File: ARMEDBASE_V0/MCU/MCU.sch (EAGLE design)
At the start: 23 parts, among them IC1 REG1117, K1 CQ1-12V, Q2 2N3904

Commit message: mcu
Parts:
- added C3, C4: 22pF, SparkFun-Capacitors:CAP0805
- added C5: 10nF, SparkFun-Capacitors:CAP0805
- added D2: (no value), SparkFun-DiscreteSemi:DIODESMA
- added IC2: MEGA8-P, atmel:MEGA8-P
- added LOGO1: OSHW-LOGOL, SparkFun-Aesthetics:OSHW-LOGOL
- added Q1: 20Mhz, crystal:CRYSTALSM49
- added Q3: 2N3904, semicon-smd-ipc:NPN-TRANSISTOR_SOT23
- added R11, R9: 1K, SparkFun-Passives:RESISTOR0805-RES
- added S2: SWITCH-MOMENTARY-2PTH, SparkFun-Electromechanical:SWITCH-MOMENTARY-2PTH
- added SV1: 5v, con-lstb:MA04-1
- S1: device SparkFun-Electromechanical:SWITCH-SPDTSMD2 -> switch:255SB
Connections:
- new net N$1: J2.2, K12.S
- new net N$21: C3.2, IC2.PB6(XTAL1/TOSC1), Q1.2
- new net N$23: C4.2, IC2.PB7(XTAL2/TOSC2), Q1.1
- new net N$24: C5.2, IC2.PC6(/RESET), R9.2, S2.1
- new net N$5: D2.A, K11.1, Q3.C
- new net N$6: Q3.B, R11.1
- new net N$9: IC2.PD7(AIN1), R11.2
- net GND: now also C3.1, C4.1, C5.1, IC2.GND, IC2.GND@1, K12.P, Q3.E, S2.2
- net RX: now also IC2.PD0(RXD)
- net TX: now also IC2.PD1(TXD)
- net VCC12V: now also D2.C, J2.1, K11.2
- net VCC5V: now also IC2.AVCC, IC2.VCC@1, R9.1
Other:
- moved on the sheet: C1, C2, D1, IC1, J1, J2, K1, LED1, R1, R2, R3, R8

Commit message: 7805
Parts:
- removed IC1: REG1117, burr-brown:REG1117
- added IC3: (no value), SparkFun-PowerIC:V_REG_78XX-TO-220
- added X1: (no value), con-berg:PN87520
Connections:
- removed net N$1: J2.2, K12.S
- net GND: now also IC3.GND; no longer IC1.GND, K12.P
- net N$5: now also J2.1; no longer K11.1
- net VCC12V: now also IC3.IN, J2.2; no longer IC1.VIN, J2.1, K11.2
- net VCC5V: now also IC3.OUT; no longer IC1.VOUT
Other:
- moved on the sheet: C3, C4, C5, D2, IC2, J2, K1, Q1, Q3, R11, R9, S2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

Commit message: usb
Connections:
- net GND: now also X1.4
- net VCC5V: now also X1.1
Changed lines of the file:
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@@
 <part name="X1" library="con-berg" deviceset="PN87520" device=""/>
 <part name="IC3" library="SparkFun-PowerIC" deviceset="V_REG_78XX" device="-TO-220"/>
+<part name="GND4" library="SparkFun-Aesthetics" deviceset="GND" device=""/>
 </parts>
 <sheets>
@@
 <instance part="X1" gate="G$1" x="144.78" y="134.62"/>
 <instance part="IC3" gate="G$1" x="66.04" y="86.36"/>
+<instance part="GND4" gate="1" x="129.54" y="132.08" rot="R270"/>
 </instances>
 <busses>
@@
 <junction x="127" y="38.1"/>
 <junction x="157.48" y="38.1"/>
+</segment>
+<segment>
+<pinref part="X1" gate="G$1" pin="1"/>
+<wire x1="142.24" y1="139.7" x2="132.08" y2="139.7" width="0.1524" layer="91"/>
+<label x="132.08" y="139.7" size="1.778" layer="95" rot="R180" xref="yes"/>
 </segment>
 </net>
@@
 <pinref part="GND5" gate="1" pin="GND"/>
 </segment>
+<segment>
+<pinref part="GND4" gate="1" pin="GND"/>
+<pinref part="X1" gate="G$1" pin="4"/>
+<wire x1="132.08" y1="132.08" x2="142.24" y2="132.08" width="0.1524" layer="91"/>
+</segment>
 </net>

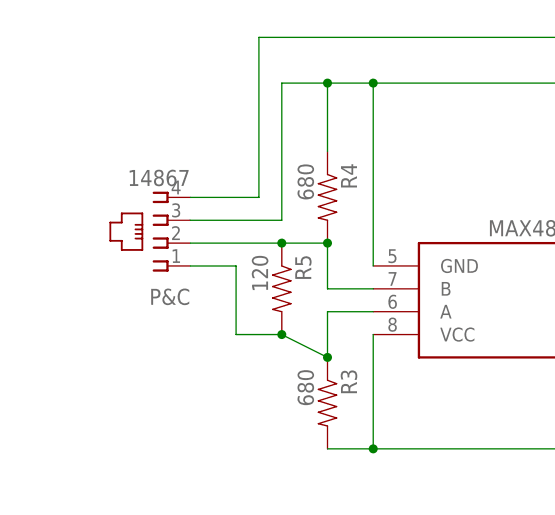
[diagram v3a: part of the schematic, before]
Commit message: modbus in-out
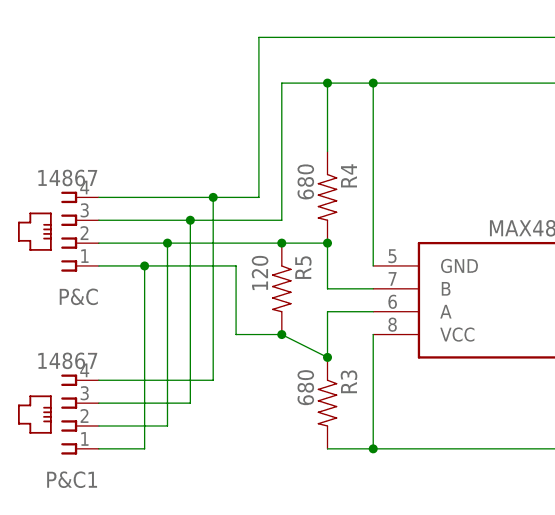
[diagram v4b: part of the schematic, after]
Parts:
- added P&C1: 14867, con-4ucon:14867
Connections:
- net GND: now also P&C1.3
- net N$7: now also P&C1.2
- net N$8: now also P&C1.1
- net VCC12V: now also P&C1.4
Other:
- moved on the sheet: P&C
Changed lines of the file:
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@@
 <part name="IC3" library="SparkFun-PowerIC" deviceset="V_REG_78XX" device="-TO-220"/>
 <part name="GND4" library="SparkFun-Aesthetics" deviceset="GND" device=""/>
+<part name="P&amp;C1" library="con-4ucon" deviceset="14867" device=""/>
 </parts>
 <sheets>
@@
 <instance part="R1" gate="G$1" x="86.36" y="15.24" rot="R270"/>
 <instance part="Q2" gate="G$1" x="78.74" y="40.64" rot="R180"/>
-<instance part="P&amp;C" gate="G$1" x="22.86" y="35.56" rot="R180"/>
+<instance part="P&amp;C" gate="G$1" x="12.7" y="35.56" rot="R180"/>
 <instance part="U$1" gate="G$1" x="60.96" y="27.94" rot="R180"/>
 <instance part="R2" gate="G$1" x="78.74" y="15.24" rot="R270"/>
@@
 <instance part="IC3" gate="G$1" x="66.04" y="86.36"/>
 <instance part="GND4" gate="1" x="129.54" y="132.08" rot="R270"/>
+<instance part="P&amp;C1" gate="G$1" x="12.7" y="15.24" rot="R180"/>
 </instances>
 <busses>
@@
 <pinref part="GND2" gate="1" pin="GND"/>
 <pinref part="P&amp;C" gate="G$1" pin="3"/>
+<wire x1="15.24" y1="35.56" x2="25.4" y2="35.56" width="0.1524" layer="91"/>
 <wire x1="25.4" y1="35.56" x2="35.56" y2="35.56" width="0.1524" layer="91"/>
 <wire x1="35.56" y1="35.56" x2="35.56" y2="50.8" width="0.1524" layer="91"/>
 <wire x1="35.56" y1="50.8" x2="40.64" y2="50.8" width="0.1524" layer="91"/>
 <junction x="40.64" y="50.8"/>
+<wire x1="25.4" y1="35.56" x2="25.4" y2="15.24" width="0.1524" layer="91"/>
+<pinref part="P&amp;C1" gate="G$1" pin="3"/>
+<wire x1="25.4" y1="15.24" x2="15.24" y2="15.24" width="0.1524" layer="91"/>
+<junction x="25.4" y="35.56"/>
 </segment>
 <segment>
@@
 <segment>
 <pinref part="P&amp;C" gate="G$1" pin="4"/>
-<wire x1="25.4" y1="38.1" x2="33.02" y2="38.1" width="0.1524" layer="91"/>
+<wire x1="15.24" y1="38.1" x2="27.94" y2="38.1" width="0.1524" layer="91"/>
 <wire x1="33.02" y1="38.1" x2="33.02" y2="55.88" width="0.1524" layer="91"/>
 <wire x1="33.02" y1="55.88" x2="104.14" y2="55.88" width="0.1524" layer="91"/>
 <label x="104.14" y="55.88" size="1.778" layer="95" xref="yes"/>
+<wire x1="33.02" y1="38.1" x2="27.94" y2="38.1" width="0.1524" layer="91"/>
+<wire x1="27.94" y1="38.1" x2="27.94" y2="17.78" width="0.1524" layer="91"/>
+<pinref part="P&amp;C1" gate="G$1" pin="4"/>
+<wire x1="27.94" y1="17.78" x2="15.24" y2="17.78" width="0.1524" layer="91"/>
+<junction x="27.94" y="38.1"/>
 </segment>
 <segment>
@@
 <wire x1="45.72" y1="27.94" x2="40.64" y2="27.94" width="0.1524" layer="91"/>
 <wire x1="40.64" y1="27.94" x2="40.64" y2="33.02" width="0.1524" layer="91"/>
-<wire x1="35.56" y1="33.02" x2="25.4" y2="33.02" width="0.1524" layer="91"/>
+<wire x1="35.56" y1="33.02" x2="22.86" y2="33.02" width="0.1524" layer="91"/>
 <pinref part="P&amp;C" gate="G$1" pin="2"/>
 <junction x="35.56" y="33.02"/>
+<wire x1="22.86" y1="33.02" x2="15.24" y2="33.02" width="0.1524" layer="91"/>
+<wire x1="22.86" y1="33.02" x2="22.86" y2="12.7" width="0.1524" layer="91"/>
+<pinref part="P&amp;C1" gate="G$1" pin="2"/>
+<wire x1="22.86" y1="12.7" x2="15.24" y2="12.7" width="0.1524" layer="91"/>
+<junction x="22.86" y="33.02"/>
 </segment>
 </net>
@@
 <junction x="40.64" y="20.32"/>
 <pinref part="P&amp;C" gate="G$1" pin="1"/>
-<wire x1="25.4" y1="30.48" x2="30.48" y2="30.48" width="0.1524" layer="91"/>
+<wire x1="15.24" y1="30.48" x2="20.32" y2="30.48" width="0.1524" layer="91"/>
+<wire x1="20.32" y1="30.48" x2="30.48" y2="30.48" width="0.1524" layer="91"/>
 <wire x1="30.48" y1="30.48" x2="30.48" y2="22.86" width="0.1524" layer="91"/>
 <junction x="35.56" y="22.86"/>
-</segment>
-</net>
+<wire x1="20.32" y1="30.48" x2="20.32" y2="10.16" width="0.1524" layer="91"/>
+<pinref part="P&amp;C1" gate="G$1" pin="1"/>
+<wire x1="20.32" y1="10.16" x2="15.24" y2="10.16" width="0.1524" layer="91"/>
+<junction x="20.32" y="30.48"/>
+</segment>
+</net>

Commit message: MCU almost
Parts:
- removed J3, J4, J5: (no value), con-amp:MTA02-156
- removed K1: CQ1-12V, relay:CQ1-12V
- added F1: 1.5A, special:FUSE
- added SV2: (no value), con-lstb:MA08-1
- added SV3, SV5: 5v, con-lstb:MA04-1
- added SV4: (no value), con-lstb:MA07-1
- Q1: value 20Mhz -> 16Mhz
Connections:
- new net KP1: IC2.PC1(ADC1), SV4.1
- new net KP2: IC2.PC0(ADC0), SV4.2
- new net KP3: IC2.PB5(SCK), SV4.3
- new net KP4: IC2.PB2(SS/OC1B), SV4.4
- new net KP5: IC2.PB1(OC1A), SV4.5
- new net KP6: IC2.PB0(ICP), SV4.6
- new net KP7: IC2.PD6(AIN0), SV4.7
- new net LCDD4: IC2.PD5(T1), SV3.4
- new net LCDD5: IC2.PD4(XCK/T0), SV3.3
- new net LCDD6: IC2.PD3(INT1), SV3.2
- new net LCDD7: IC2.PD2(INT0), SV3.1
- new net LCDEN: IC2.PB3(MOSI/OC2), SV2.1
- new net LCDRS: IC2.PB4(MISO), SV2.3
- new net N$1: C1.2, F1.1, IC3.OUT, R8.2
- new net N$15: IC2.PC2(ADC2), SV1.1
- new net N$16: IC2.PC3(ADC3), SV1.2
- new net N$17: IC2.PC4(ADC4/SDA), SV1.3
- new net N$18: IC2.PC5(ADC5/SCL), SV1.4
- net GND: now also SV2.2, SV2.4, SV2.6, SV5.1, SV5.2
- net VCC12V: now also SV5.4
- net VCC5V: now also F1.2, SV2.5, SV5.3; no longer C1.2, IC3.OUT, R8.2
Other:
- moved on the sheet: D2, J2, Q3, R11, SV1, X1

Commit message: net class settings
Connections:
- net N$1: now also F1.2, IC3.IN; no longer C1.2, F1.1, IC3.OUT, R8.2
- net VCC12V: now also F1.1; no longer IC3.IN
- net VCC5V: now also C1.2, IC3.OUT, R8.2; no longer F1.2
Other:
- note added: "CONTROLLER"
- note added: "KEYPAD"
- note added: "LCD"
- note added: "MODBUS + RTU POWER OUT"
- note added: "POWER IN"
- note added: "POWER OUT"
- note added: "SIREN"
- moved on the sheet: C1, D2, F1, IC3, J2, LED1, Q3, R11, R8, SV2, SV4

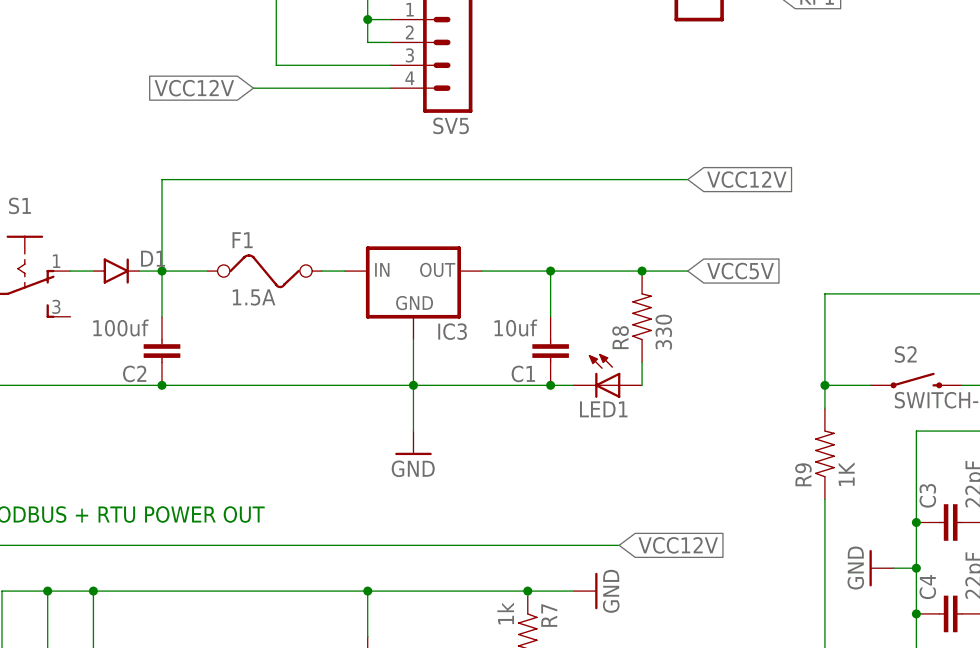
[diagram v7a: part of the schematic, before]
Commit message: fuse replace
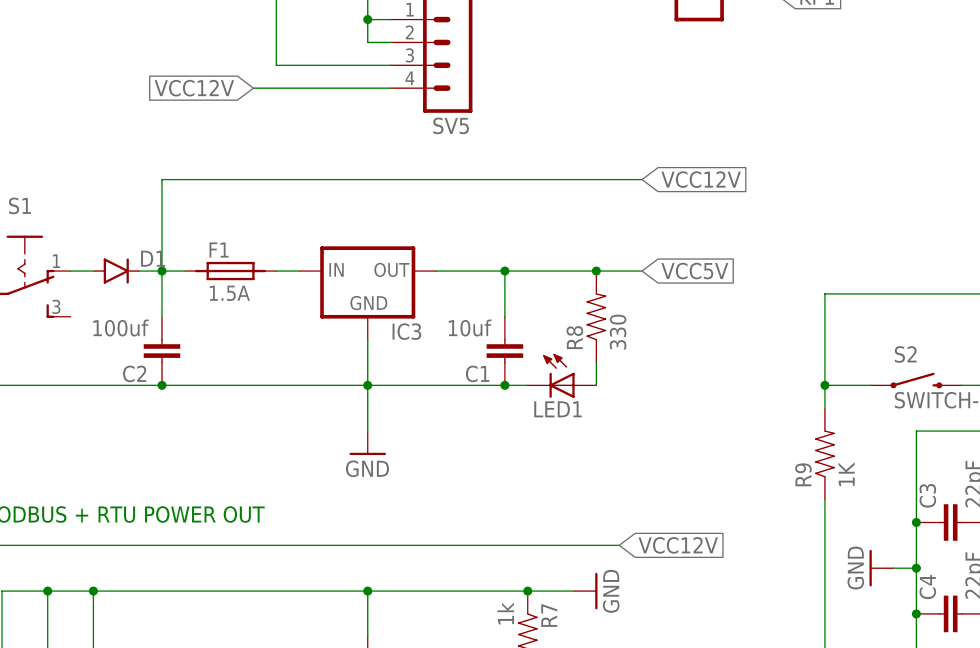
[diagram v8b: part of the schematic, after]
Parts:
- F1: device special:FUSE -> _hhn_PtcFuses_Siba_r500_Ozan:SIBA194600
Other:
- moved on the sheet: C1, IC3, LED1, R8
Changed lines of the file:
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@@
 </variantdefs>
 <classes>
-<class number="0" name="default" width="0.4" drill="0.5">
+<class number="0" name="default" width="0.3" drill="0.5">
 <clearance class="0" value="0.25"/>
 </class>
@@
 <part name="GND4" library="SparkFun-Aesthetics" deviceset="GND" device=""/>
 <part name="P&amp;C1" library="con-4ucon" deviceset="14867" device=""/>
-<part name="F1" library="special" deviceset="FUSE" device="" value="1.5A"/>
+<part name="F1" library="_hhn_PtcFuses_Siba_r500_Ozan" deviceset="SIBA194600*" device="" value="1.5A"/>
 <part name="SV2" library="con-lstb" deviceset="MA08-1" device=""/>
 <part name="SV3" library="con-lstb" deviceset="MA04-1" device="" value="5v"/>
@@
 <instances>
 <instance part="J1" gate="G$1" x="25.4" y="81.28"/>
-<instance part="C1" gate="G$1" x="96.52" y="78.74" rot="R180"/>
-<instance part="LED1" gate="G$1" x="104.14" y="73.66" rot="R270"/>
+<instance part="C1" gate="G$1" x="91.44" y="78.74" rot="R180"/>
+<instance part="LED1" gate="G$1" x="99.06" y="73.66" rot="R270"/>
 <instance part="D1" gate="G$1" x="48.26" y="86.36"/>
-<instance part="GND1" gate="1" x="81.28" y="66.04"/>
+<instance part="GND1" gate="1" x="76.2" y="66.04"/>
 <instance part="SUPPLY1" gate="G$1" x="22.86" y="91.44" rot="R90"/>
 <instance part="S1" gate="1" x="38.1" y="86.36" rot="R270"/>
 <instance part="C2" gate="G$1" x="53.34" y="78.74" rot="R180"/>
-<instance part="R8" gate="G$1" x="106.68" y="81.28" rot="R90"/>
+<instance part="R8" gate="G$1" x="101.6" y="81.28" rot="R90"/>
 <instance part="J2" gate="G$1" x="256.54" y="43.18"/>
 <instance part="R1" gate="G$1" x="86.36" y="15.24" rot="R270"/>
@@
 <instance part="GND5" gate="1" x="266.7" y="25.4" rot="R90"/>
 <instance part="X1" gate="G$1" x="81.28" y="127"/>
-<instance part="IC3" gate="G$1" x="81.28" y="86.36"/>
+<instance part="IC3" gate="G$1" x="76.2" y="86.36"/>
 <instance part="GND4" gate="1" x="71.12" y="124.46" rot="R270"/>
 <instance part="P&amp;C1" gate="G$1" x="12.7" y="15.24" rot="R180"/>
-<instance part="F1" gate="G$1" x="66.04" y="86.36"/>
+<instance part="F1" gate="G$1" x="60.96" y="86.36"/>
 <instance part="SV2" gate="1" x="172.72" y="106.68"/>
 <instance part="SV3" gate="1" x="172.72" y="134.62"/>
@@
 </segment>
 <segment>
-<label x="111.76" y="86.36" size="1.778" layer="95" xref="yes"/>
+<label x="106.68" y="86.36" size="1.778" layer="95" xref="yes"/>
 <pinref part="C1" gate="G$1" pin="2"/>
-<wire x1="96.52" y1="86.36" x2="96.52" y2="81.28" width="0.1524" layer="91"/>
-<wire x1="96.52" y1="86.36" x2="106.68" y2="86.36" width="0.1524" layer="91"/>
+<wire x1="91.44" y1="86.36" x2="91.44" y2="81.28" width="0.1524" layer="91"/>
+<wire x1="91.44" y1="86.36" x2="101.6" y2="86.36" width="0.1524" layer="91"/>
 <pinref part="R8" gate="G$1" pin="2"/>
-<junction x="106.68" y="86.36"/>
-<junction x="96.52" y="86.36"/>
+<junction x="101.6" y="86.36"/>
+<junction x="91.44" y="86.36"/>
 <pinref part="IC3" gate="G$1" pin="OUT"/>
-<wire x1="88.9" y1="86.36" x2="96.52" y2="86.36" width="0.1524" layer="91"/>
-<wire x1="106.68" y1="86.36" x2="111.76" y2="86.36" width="0.1524" layer="91"/>
+<wire x1="83.82" y1="86.36" x2="91.44" y2="86.36" width="0.1524" layer="91"/>
+<wire x1="101.6" y1="86.36" x2="106.68" y2="86.36" width="0.1524" layer="91"/>
 </segment>
 <segment>
@@
 <junction x="53.34" y="73.66"/>
 <wire x1="30.48" y1="73.66" x2="53.34" y2="73.66" width="0.1524" layer="91"/>
-<wire x1="53.34" y1="73.66" x2="81.28" y2="73.66" width="0.1524" layer="91"/>
+<wire x1="53.34" y1="73.66" x2="76.2" y2="73.66" width="0.1524" layer="91"/>
 <pinref part="C1" gate="G$1" pin="1"/>
-<junction x="96.52" y="73.66"/>
+<junction x="91.44" y="73.66"/>
 <pinref part="GND1" gate="1" pin="GND"/>
-<wire x1="96.52" y1="73.66" x2="81.28" y2="73.66" width="0.1524" layer="91"/>
-<wire x1="81.28" y1="73.66" x2="81.28" y2="68.58" width="0.1524" layer="91"/>
-<junction x="81.28" y="73.66"/>
+<wire x1="91.44" y1="73.66" x2="76.2" y2="73.66" width="0.1524" layer="91"/>
+<wire x1="76.2" y1="73.66" x2="76.2" y2="68.58" width="0.1524" layer="91"/>
+<junction x="76.2" y="73.66"/>
 <pinref part="LED1" gate="G$1" pin="C"/>
-<wire x1="96.52" y1="73.66" x2="99.06" y2="73.66" width="0.1524" layer="91"/>
+<wire x1="91.44" y1="73.66" x2="93.98" y2="73.66" width="0.1524" layer="91"/>
 <pinref part="J1" gate="G$1" pin="1"/>
 <wire x1="30.48" y1="78.74" x2="30.48" y2="73.66" width="0.1524" layer="91"/>
 <pinref part="IC3" gate="G$1" pin="GND"/>
-<wire x1="81.28" y1="78.74" x2="81.28" y2="73.66" width="0.1524" layer="91"/>
+<wire x1="76.2" y1="78.74" x2="76.2" y2="73.66" width="0.1524" layer="91"/>
 </segment>
 <segment>
@@
 <pinref part="R8" gate="G$1" pin="1"/>
 <pinref part="LED1" gate="G$1" pin="A"/>
-<wire x1="106.68" y1="73.66" x2="106.68" y2="76.2" width="0.1524" layer="91"/>
+<wire x1="101.6" y1="73.66" x2="101.6" y2="76.2" width="0.1524" layer="91"/>
 </segment>
 </net>
@@
 <junction x="53.34" y="86.36"/>
 <wire x1="53.34" y1="86.36" x2="53.34" y2="96.52" width="0.1524" layer="91"/>
-<wire x1="53.34" y1="96.52" x2="111.76" y2="96.52" width="0.1524" layer="91"/>
-<label x="111.76" y="96.52" size="1.778" layer="95" xref="yes"/>
-<wire x1="53.34" y1="86.36" x2="58.42" y2="86.36" width="0.1524" layer="91"/>
+<wire x1="53.34" y1="96.52" x2="106.68" y2="96.52" width="0.1524" layer="91"/>
+<label x="106.68" y="96.52" size="1.778" layer="95" xref="yes"/>
+<wire x1="53.34" y1="86.36" x2="55.88" y2="86.36" width="0.1524" layer="91"/>
 <pinref part="F1" gate="G$1" pin="1"/>
 </segment>
@@
 <pinref part="IC3" gate="G$1" pin="IN"/>
 <pinref part="F1" gate="G$1" pin="2"/>
-<wire x1="71.12" y1="86.36" x2="73.66" y2="86.36" width="0.1524" layer="91"/>
-</segment>
-</net>
+<wire x1="66.04" y1="86.36" x2="68.58" y2="86.36" width="0.1524" layer="91"/>
+</segment>
+</net>
